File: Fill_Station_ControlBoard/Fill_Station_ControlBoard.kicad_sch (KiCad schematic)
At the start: 69 parts, among them J1 Conn_01x03, J2 Conn_01x03, J3 USB_C_Receptacle_USB2.0_14P, J4 DE9_Pins, J5 Micro_SD_Card_Det1, J6 RJ45_Wuerth_7499010211A, SW1 CK_KMS2xxG, U1 STM32H747IITx, U2 USBLC6-2SC6, U3 MCP2561-E-P, U5 LAN8742A, Y1 Crystal

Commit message: Restructure + phy ethernet
Finaliser le phy ethernet et changé pour hyerarchical sheets
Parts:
- removed C10: 470pF, symbol Device:C
- removed C11, C12, C13, C21, C22, C23, C24, C25: C, symbol Device:C
- removed C6: 0.1uF, symbol Device:C
- removed C7: 10uF, symbol Device:C
- removed C9: 1uF, symbol Device:C
- removed CBypass1, CBypass2, CBypass3, CBypass4, Cf: ~, symbol Device:C
- removed D1, D2: BAV99, Package_TO_SOT_SMD:SOT-23, symbol Diode:BAV99
- removed D3: 6.4V, symbol Device:D_Zener
- removed D4: D, symbol Device:D
- removed D5, D6: ESD9B3.3ST5G, Diode_SMD:D_SOD-923, symbol Diode:ESD9B3.3ST5G
- removed F1, F2: Fuse, symbol Device:Fuse
- removed F3: Polyfuse, symbol Device:Polyfuse
- removed J1, J2: Conn_01x03, symbol Connector_Generic:Conn_01x03
- removed J3: USB_C_Receptacle_USB2.0_14P, symbol Connector:USB_C_Receptacle_USB2.0_14P
- removed J4: DE9_Pins, symbol Connector:DE9_Pins
- removed J5: Micro_SD_Card_Det1, symbol Connector:Micro_SD_Card_Det1
- removed J6: RJ45_Wuerth_7499010211A, Connector_RJ:RJ45_Wuerth_7499010211A_Horizontal, symbol Connector:RJ45_Wuerth_7499010211A
- removed R1, R2, R5: 10k, symbol Device:R_US
- removed R10, R11, R12, R13, R9: 47k, symbol Device:R_US
- removed R3, R4: 5.1k, symbol Device:R_US
- removed R6: R, symbol Device:R_US
- removed R7: 0, symbol Device:R_US
- removed R8: 12.1k, symbol Device:R_US
- removed U2: USBLC6-2SC6, Package_TO_SOT_SMD:SOT-23-6, symbol Power_Protection:USBLC6-2SC6
- removed U3: MCP2561-E-P, Package_DIP:DIP-8_W7.62mm, symbol Interface_CAN_LIN:MCP2561-E-P
- removed U5: LAN8742A, Package_DFN_QFN:VQFN-24-1EP_4x4mm_P0.5mm_EP2.5x2.5mm_ThermalVias, symbol Interface_Ethernet:LAN8742A
- added R27: 100k, symbol Device:R_US
- added SW2: BOOT, symbol Switch:SW_Push_SPDT
- C1, C4: value 0.1uF -> *
- C14, C15, C16, C17, C18, C19, C20, C5, C8: value C -> *
- C2, C3: value 1uF -> *
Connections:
- net Eth.TXD0: now also U1.157 (PG13); no longer U1.85 (PB12)
- net Eth.TXEN: now also U1.155 (PG11); no longer U1.79 (PB11)
- net GND: now also SW2.1 (A); no longer R14.2, SW1.SH (B)
- net 3V3: now reaches C2.1
- net 3V3: now also C14.1, C15.1, C16.1, C17.1, C18.1, C3.1, C4.1, C5.1, C8.1, R14.1, U1.113 (VDD), U1.126 (VDD), U1.13 (VDD), U1.136 (VDD), U1.152 (VDD), U1.160 (VDD), U1.176 (VDD), U1.25 (VDD), U1.44 (VDD), U1.48 (VDD), U1.65 (VDD), U1.7 (VDD), U1.71 (VDD), U1.84 (VDD), U1.92 (VDD), U1.99 (VDD), R27.1; no longer C1.1
- net at U1.167 (BOOT0): now also SW2.2 (B); no longer R14.1
- net Eth.CLKIN: now reaches C26.2, R15.1, Y1.2
- net Eth.RST: now reaches U1.1 (PE2)
- net Eth.RXER: now reaches U1.110 (PG2)
- net at SW1.2, U1.33 (NRST): now also R27.2; no longer C5.1
- net Eth.REFCLKO: now reaches U1.42 (PA1)
- removed net +3.3V: C14.1, C15.1, C16.1, C17.1, C18.1, C19.1, C20.1, C8.1, U1.113 (VDD), U1.126 (VDD), U1.13 (VDD), U1.136 (VDD), U1.152 (VDD), U1.160 (VDD), U1.176 (VDD), U1.25 (VDD), U1.40 (VDDA), U1.44 (VDD), U1.48 (VDD), U1.65 (VDD), U1.7 (VDD), U1.71 (VDD), U1.84 (VDD), U1.92 (VDD), U1.99 (VDD)
- net Servo.CTRL1: no longer names the net of U1.124 (PC8)
- net Servo.CTRL2: no longer names the net of U1.125 (PC9)
- new net: R14.2, SW2.3 (C)
- new net 3V3A: C1.1, C19.1, C20.1, U1.40 (VDDA)
- no-connect marks 1 -> 0
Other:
- added sheet Communication (Connecteurs.kicad_sch)
- added sheet Control (untitled.kicad_sch)
- added sheet Storage (Storage.kicad_sch)
- note added: "Découplage"
- note added: "pins ethernet doivent être high impedence lors de la configuaration ou reset du phy"
- note removed: "CAN"
- note removed: "Eth"
- note removed: "Power"
- note removed: "SD"
- note removed: "Servo"
- note removed: "USBC"
- moved on the sheet: C26, C27, R14, R15, R16, SW1, U1, Y1

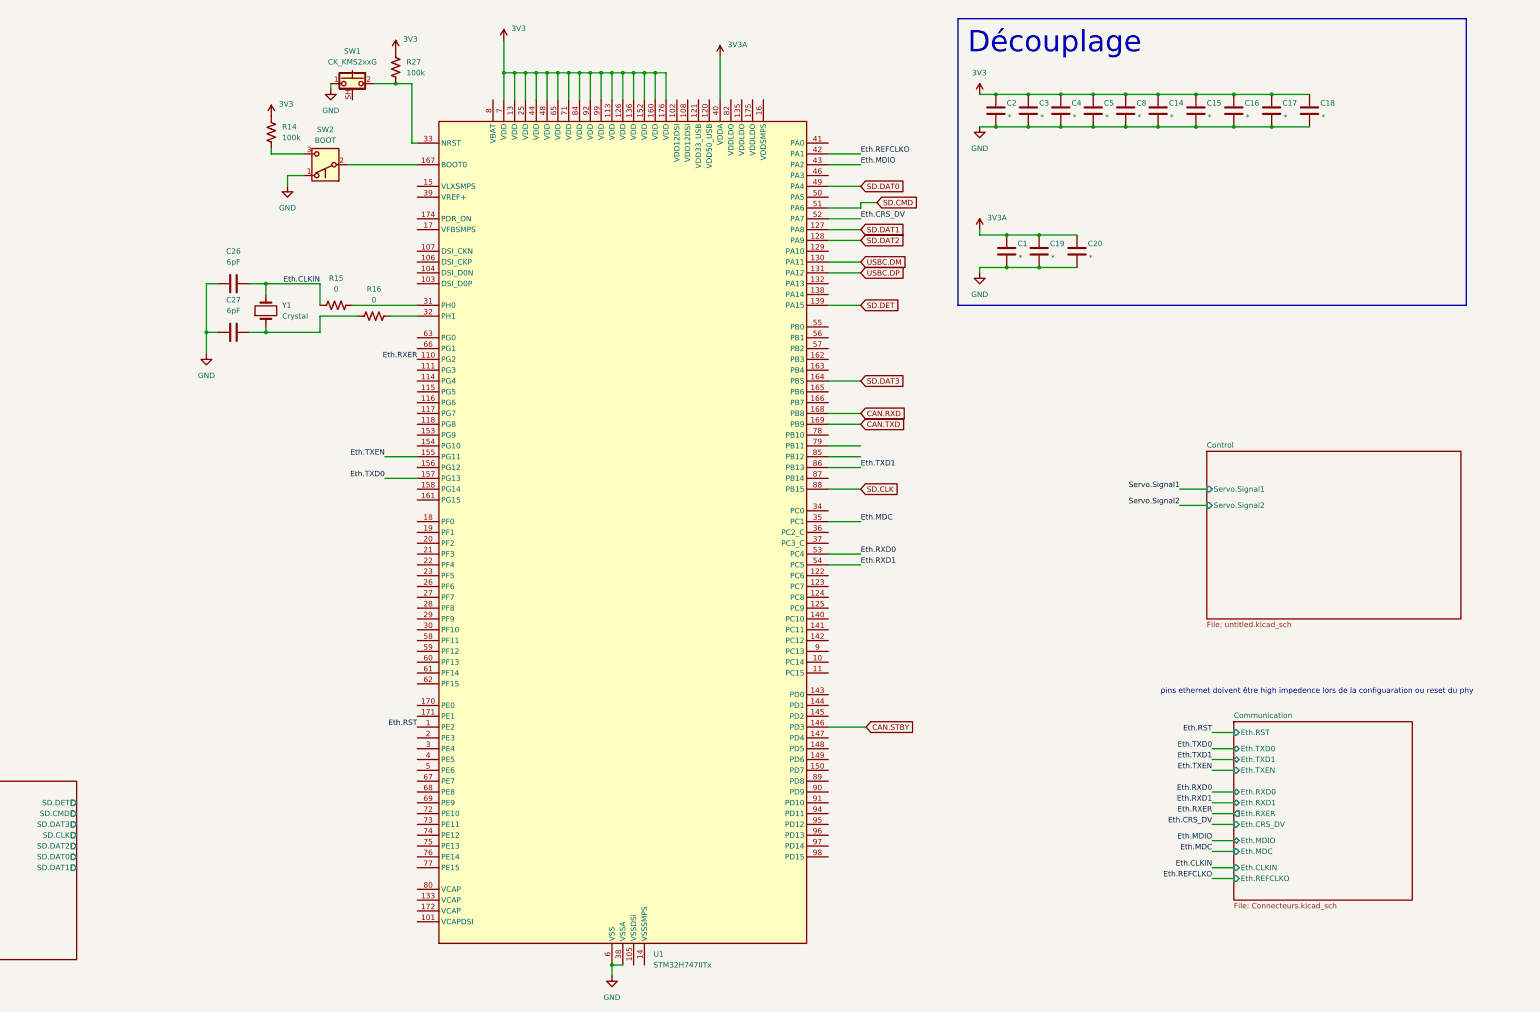
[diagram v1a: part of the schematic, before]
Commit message: petites modifs pour ethernet + usb
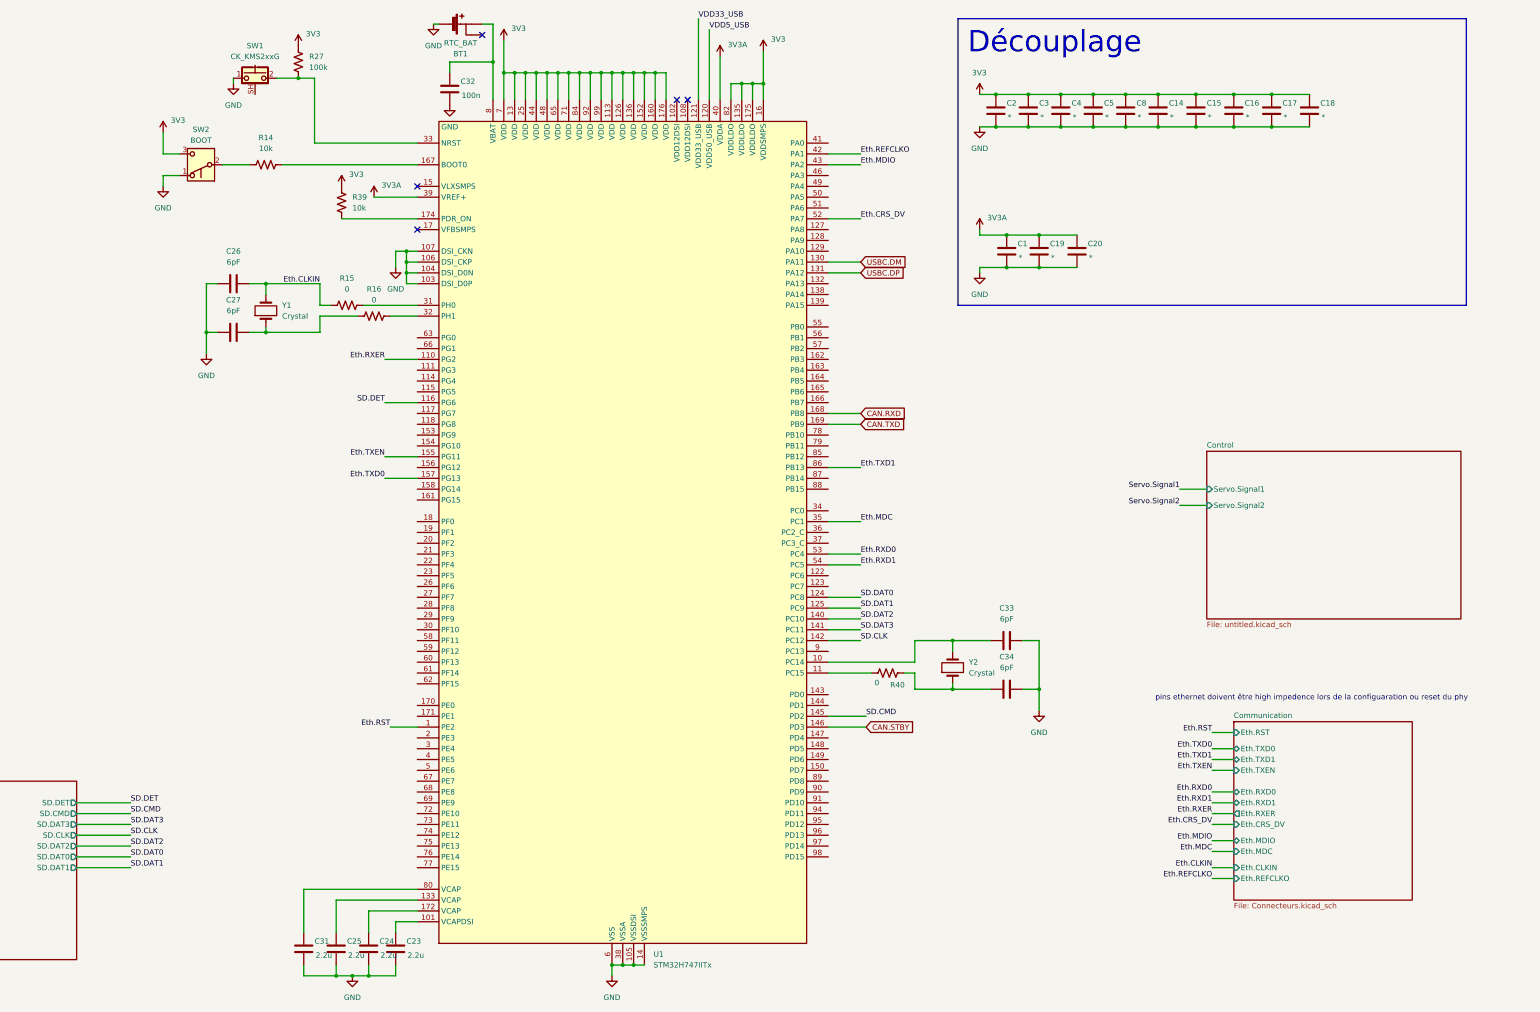
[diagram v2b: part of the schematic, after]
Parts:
- added BT1: RTC_BAT, 0CSL_D1_V1:BatteryHolder_BHX1_1025, symbol 0CSL_D1_V1:Battery_Holder_1025
- added C23, C24, C25, C31: 2.2u, symbol Device:C
- added C32: 100n, symbol Device:C
- added C33, C34: 6pF, symbol Device:C
- added R39: 10k, symbol Device:R_US
- added R40: 0, symbol Device:R_US
- added Y2: Crystal, Crystal:Crystal_SMD_3225-4Pin_3.2x2.5mm, symbol Device:Crystal
- R14: value 100k -> 10k
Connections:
- net 3V3: now also SW2.3 (C), U1.135 (VDDLDO), U1.16 (VDDSMPS), U1.175 (VDDLDO), U1.82 (VDDLDO), R39.1; no longer R14.1
- net 3V3A: now also U1.39 (VREF+)
- net GND: now also U1.103 (DSI_D0P), U1.104 (DSI_D0N), U1.105 (VSSDSI), U1.106 (DSI_CKP), U1.107 (DSI_CKN), U1.109 (VSSDSI), U1.14 (VSSSMPS), BT1.2 (-), C23.2, C24.2, C25.2, C31.2, C32.2, C33.2, C34.2
- net SD.CLK: now also U1.142 (PC12); no longer U1.88 (PB15)
- net SD.CMD: now also U1.145 (PD2); no longer U1.51 (PA6)
- net SD.DAT0: now also U1.124 (PC8); no longer U1.49 (PA4)
- net SD.DAT1: now also U1.125 (PC9); no longer U1.127 (PA8)
- net SD.DAT2: now also U1.140 (PC10); no longer U1.128 (PA9)
- net SD.DAT3: now also U1.141 (PC11); no longer U1.164 (PB5)
- net SD.DET: now also U1.116 (PG6); no longer U1.139 (PA15)
- net at R14.2: now also U1.167 (BOOT0); no longer SW2.3 (C)
- net at U1.10 (PC14): now also C33.1, Y2.2
- net at U1.101 (VCAPDSI): now also C23.1
- net at U1.11 (PC15): now also R40.2
- net VDD5_USB: now reaches U1.120 (VDD50_USB)
- net VDD33_USB: now reaches U1.121 (VDD33_USB)
- net at U1.133 (VCAP): now also C25.1
- net at SW2.2 (B): now also R14.1; no longer U1.167 (BOOT0)
- net at U1.172 (VCAP): now also C24.1
- net at U1.174 (PDR_ON): now also R39.2
- net at U1.8 (VBAT): now also BT1.1 (+), C32.1
- net at U1.80 (VCAP): now also C31.1
- new net: C34.1, R40.1, Y2.1
- no-connect marks 0 -> 5
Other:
- moved on the sheet: R14, R15, R27, SW1, SW2

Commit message: heater
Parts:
- C33, C34: value 6pF -> *
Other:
- added sheet Heaters (Heaters.kicad_sch)
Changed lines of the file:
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@@
 	(wire
 		(pts
-			(xy 132.08 58.42) (xy 163.83 58.42)
-		)
-		(stroke
-			(width 0)
-			(type default)
-		)
-	)
-	(wire
-		(pts
 			(xy 260.35 81.28) (xy 267.97 81.28)
 		)
@@
 	(wire
 		(pts
+			(xy 132.08 58.42) (xy 163.83 58.42)
+		)
+		(stroke
+			(width 0)
+			(type default)
+		)
+	)
+	(wire
+		(pts
 			(xy 196.85 36.83) (xy 196.85 43.18)
 		)
@@
 			)
 		)
-		(property "Value" "6pF"
+		(property "Value" "*"
 			(at 302.26 165.1 90)
 			(effects
@@
 			)
 		)
-		(property "Value" "6pF"
+		(property "Value" "*"
 			(at 302.26 176.53 90)
 			(effects
@@
 				)
 			)
+		)
+	)
+	(sheet
+		(at 27.94 148.59)
+		(size 55.88 30.48)
+		(exclude_from_sim no)
+		(in_bom yes)
+		(on_board yes)
+		(dnp no)
+		(fields_autoplaced yes)
+		(stroke
+			(width 0.1524)
+			(type solid)
+		)
+		(fill
+			(color 0 0 0 0.0000)
+		)
+		(property "Sheetname" "Heaters"
+			(at 27.94 147.8784 0)
+			(effects
+				(font
+					(size 1.27 1.27)
+				)
+				(justify left bottom)
+			)
+		)
+		(property "Sheetfile" "Heaters.kicad_sch"
+			(at 27.94 179.6546 0)
+			(effects
+				(font
+					(size 1.27 1.27)
+				)
+				(justify left top)
+			)
+		)
+		(pin "GPIO6" input
+			(at 83.82 172.72 0)
+			(effects
+				(font
+					(size 1.27 1.27)
+				)
+				(justify right)
+			)
+		)
+		(pin "GPIO2" input
+			(at 83.82 157.48 0)
+			(effects
+				(font
+					(size 1.27 1.27)
+				)
+				(justify right)
+			)
+		)
+		(pin "GPIO1" input
+			(at 83.82 153.67 0)
+			(effects
+				(font
+					(size 1.27 1.27)
+				)
+				(justify right)
+			)
+		)
+		(pin "GPIO4" input
+			(at 83.82 165.1 0)
+			(effects
+				(font
+					(size 1.27 1.27)
+				)
+				(justify right)
+			)
+		)
+		(pin "GPIO5" input
+			(at 83.82 168.91 0)
+			(effects
+				(font
+					(size 1.27 1.27)
+				)
+				(justify right)
+			)
+		)
+		(pin "GPIO3" input
+			(at 83.82 161.29 0)
+			(effects
+				(font
+					(size 1.27 1.27)
+				)
+				(justify right)
+			)
+		)
+		(instances
+			(project "Fill_Station_ControlBoard"
+				(path "/eaacffe0-ee57-428e-a37e-5655e0922ccc"
+					(page "5")
+				)
+			)

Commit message: Ajouter schema de JTAG
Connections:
- net CAN.RXD: now also U1.169 (PB9); no longer U1.168 (PB8)
- net CAN.TXD: now also U1.168 (PB8); no longer U1.169 (PB9)
- net JTMS: now reaches U1.132 (PA13)
- net JTCK: now reaches U1.138 (PA14)
- net JTDI: now reaches U1.139 (PA15)
- net JTDO: now reaches U1.162 (PB3)
- net NJTRST: now reaches U1.163 (PB4)
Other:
- added sheet Connecteur (connecteur.kicad_sch)

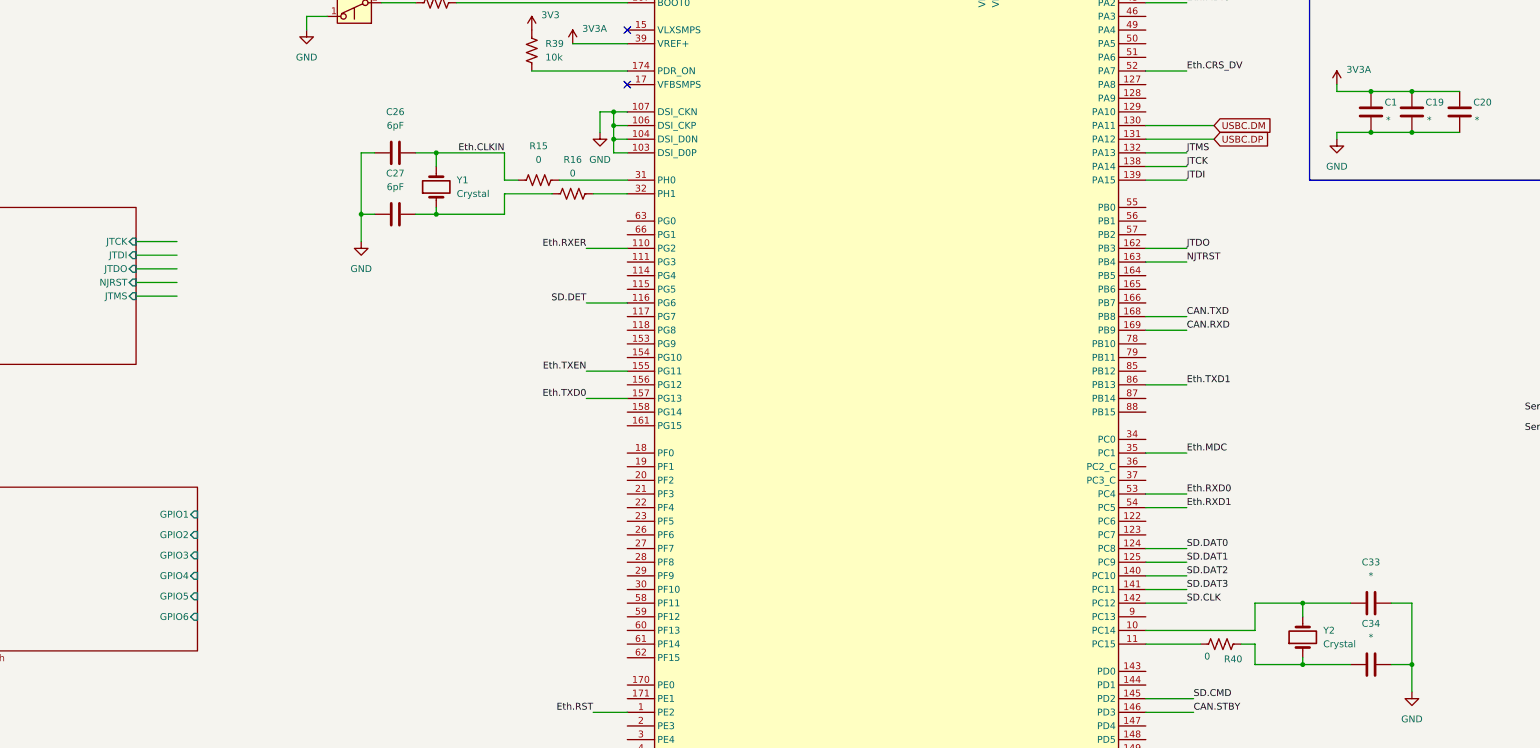
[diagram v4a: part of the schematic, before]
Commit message: Changement de CAN et quelques trucs
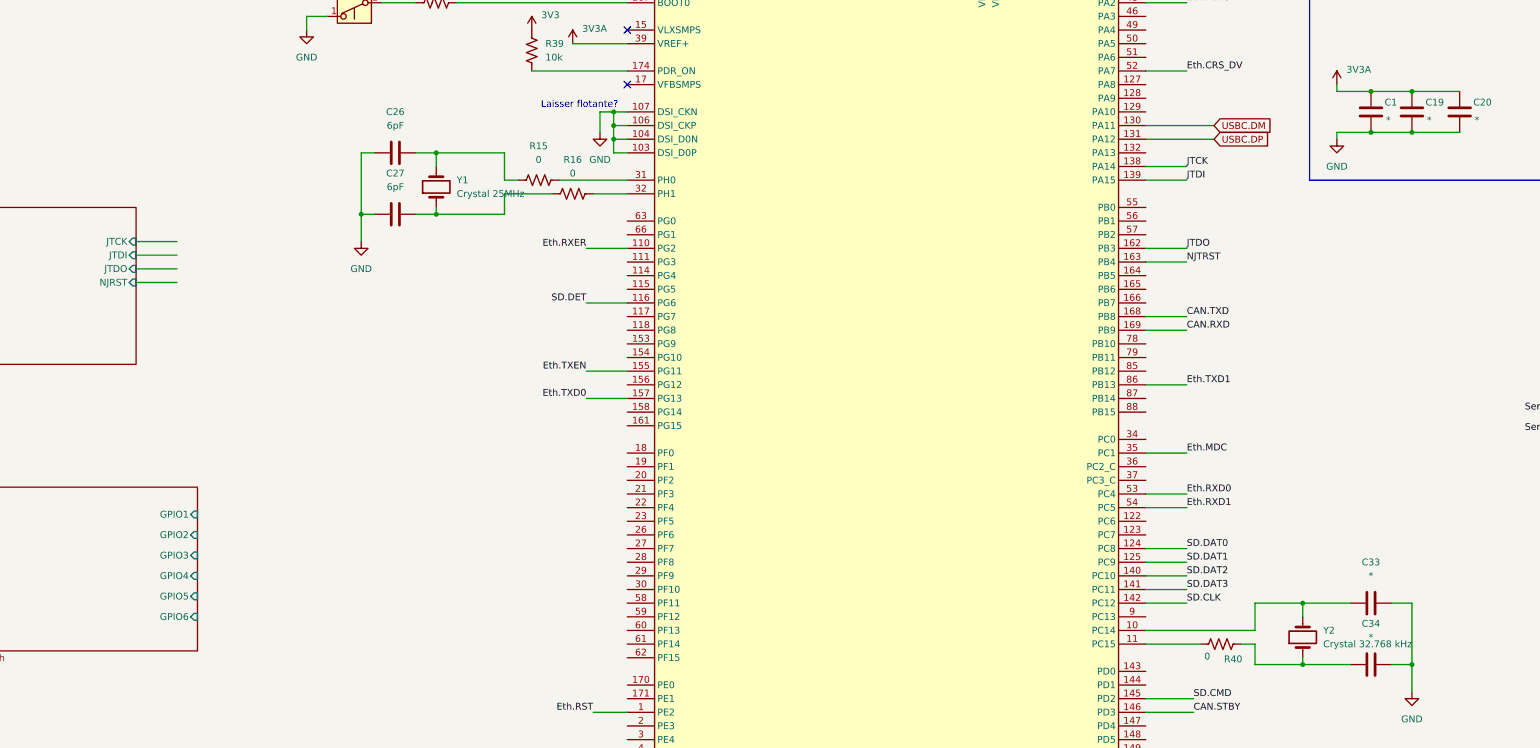
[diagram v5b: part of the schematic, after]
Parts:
- R14, R15, R16, R27, R39, R40: footprint (none) -> Resistor_SMD:R_0603_1608Metric_Pad0.98x0.95mm_HandSolder
- Y1: value Crystal -> Crystal 25MHz
- Y2: value Crystal -> Crystal 32.768 kHz
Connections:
- net Eth.CLKIN: no longer C26.2, R15.1, Y1.2
- net JTMS: no longer names the net of U1.132 (PA13)
- new net: C26.2, R15.1, Y1.2
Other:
- sheet Connecteur ports: added none; removed JTMS
- note added: "Laisser flotante?"
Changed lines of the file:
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@@
 		)
 	)
+	(text "Laisser flotante?\n"
+		(exclude_from_sim no)
+		(at 154.94 77.47 0)
+		(effects
+			(font
+				(size 1.27 1.27)
+			)
+		)
+	)
 	(text "Découplage"
 		(exclude_from_sim no)
@@
 	(wire
 		(pts
-			(xy 72.39 113.03) (xy 80.01 113.03)
-		)
-		(stroke
-			(width 0)
-			(type default)
-		)
-	)
-	(wire
-		(pts
 			(xy 245.11 31.75) (xy 245.11 39.37)
 		)
@@
 	(wire
 		(pts
-			(xy 260.35 86.36) (xy 267.97 86.36)
-		)
-		(stroke
-			(width 0)
-			(type default)
-		)
-	)
-	(wire
-		(pts
 			(xy 137.16 238.76) (xy 137.16 228.6)
 		)
@@
 		)
 	)
-	(label "Eth.CLKIN"
-		(at 140.97 86.36 180)
-		(effects
-			(font
-				(size 1.27 1.27)
-			)
-			(justify right bottom)
-		)
-	)
 	(label "SD.DET"
 		(at 96.52 208.28 0)
@@
 		)
 	)
-	(label "JTMS"
-		(at 267.97 86.36 0)
-		(effects
-			(font
-				(size 1.27 1.27)
-			)
-			(justify left bottom)
-		)
-	)
 	(label "Eth.REFCLKO"
 		(at 350.52 226.06 180)
@@
 			)
 		)
-		(property "Value" "Crystal"
+		(property "Value" "Crystal 32.768 kHz"
 			(at 293.37 177.7999 90)
 			(effects
@@
 			)
 		)
-		(property "Footprint" ""
+		(property "Footprint" "Resistor_SMD:R_0603_1608Metric_Pad0.98x0.95mm_HandSolder"
 			(at 128.524 57.404 90)
 			(effects
@@
 			)
 		)
-		(property "Footprint" ""
+		(property "Footprint" "Resistor_SMD:R_0603_1608Metric_Pad0.98x0.95mm_HandSolder"
 			(at 147.574 90.424 90)
 			(effects
@@
 			)
 		)
-		(property "Footprint" ""
+		(property "Footprint" "Resistor_SMD:R_0603_1608Metric_Pad0.98x0.95mm_HandSolder"
 			(at 136.906 34.544 90)
 			(effects
@@
 			)
 		)
-		(property "Footprint" ""
+		(property "Footprint" "Resistor_SMD:R_0603_1608Metric_Pad0.98x0.95mm_HandSolder"
 			(at 274.066 178.816 90)
 			(effects
@@
 			)
 		)
-		(property "Footprint" ""
+		(property "Footprint" "Resistor_SMD:R_0603_1608Metric_Pad0.98x0.95mm_HandSolder"
 			(at 147.066 67.564 90)
 			(effects
@@
 			)
 		)
-		(property "Value" "Crystal"
+		(property "Value" "Crystal 25MHz"
 			(at 132.08 93.9799 90)
 			(effects
@@
 			)
 		)
-		(property "Footprint" ""
+		(property "Footprint" "Resistor_SMD:R_0603_1608Metric_Pad0.98x0.95mm_HandSolder"
 			(at 153.924 92.964 90)
 			(effects
@@
 			(effects
 				(font
-					(size 1.27 1.27)
-				)
-				(justify right)
-			)
-		)
-		(pin "JTMS" input
-			(at 72.39 113.03 0)
-			(effects
-				(font
